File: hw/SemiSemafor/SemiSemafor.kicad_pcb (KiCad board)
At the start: 2 copper layers, 26.3 x 50.2 mm, 40 parts, among them J1 USB_PCB, J2 ESP-Programing_conector, SW1 SW_DIP_x01, SW2 SW_DIP_x01, U1 LD39200, U2 ESP32-C3-MINI-1

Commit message: 3D-models
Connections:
- D10 pad 1: Net-(D10-DOUT) -> Net-(D1-DOUT)
- D10 pad 3: Net-(D10-DIN) -> Net-(D1-DIN)
- D11 pad 1: Net-(D11-DOUT) -> Net-(D1-DOUT)
- D11 pad 3: Net-(D10-DOUT) -> Net-(D1-DIN)
- D12 pad 1: unconnected-(D12-DOUT-Pad1) -> Net-(D1-DOUT)
- D12 pad 3: Net-(D11-DOUT) -> Net-(D1-DIN)
- D2 pad 1: Net-(D2-DOUT) -> Net-(D1-DOUT)
- D2 pad 3: Net-(D1-DOUT) -> Net-(D1-DIN)
- D3 pad 1: Net-(D3-DOUT) -> Net-(D1-DOUT)
- D3 pad 3: Net-(D2-DOUT) -> Net-(D1-DIN)
- D4 pad 1: Net-(D4-DOUT) -> Net-(D1-DOUT)
- D4 pad 3: Net-(D3-DOUT) -> Net-(D1-DIN)
- D5 pad 1: Net-(D5-DOUT) -> Net-(D1-DOUT)
- D5 pad 3: Net-(D4-DOUT) -> Net-(D1-DIN)
- D6 pad 1: Net-(D6-DOUT) -> Net-(D1-DOUT)
- D6 pad 3: Net-(D5-DOUT) -> Net-(D1-DIN)
- D7 pad 1: Net-(D7-DOUT) -> Net-(D1-DOUT)
- D7 pad 3: Net-(D6-DOUT) -> Net-(D1-DIN)
- D8 pad 1: Net-(D8-DOUT) -> Net-(D1-DOUT)
- D8 pad 3: Net-(D7-DOUT) -> Net-(D1-DIN)
- D9 pad 1: Net-(D10-DIN) -> Net-(D1-DOUT)
- D9 pad 3: Net-(D8-DOUT) -> Net-(D1-DIN)

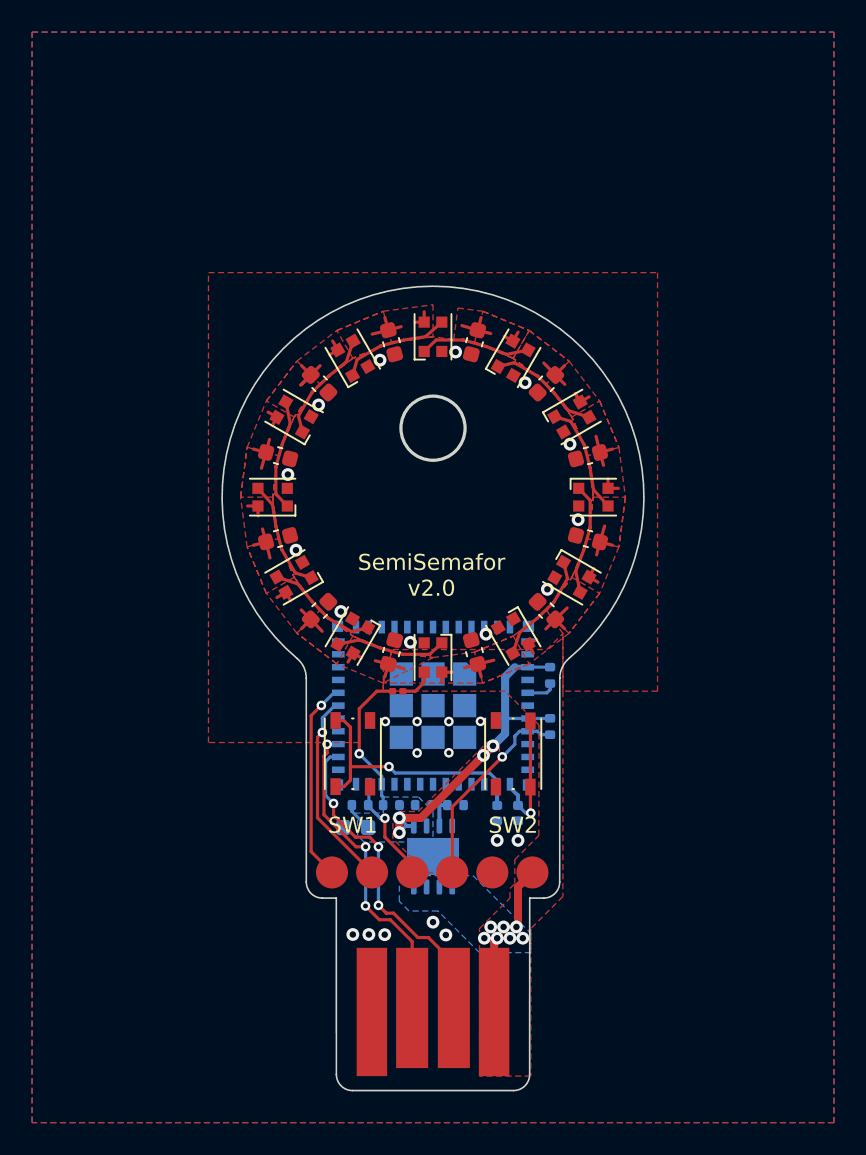
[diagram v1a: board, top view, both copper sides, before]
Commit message: Add IMU and move LED ring higher
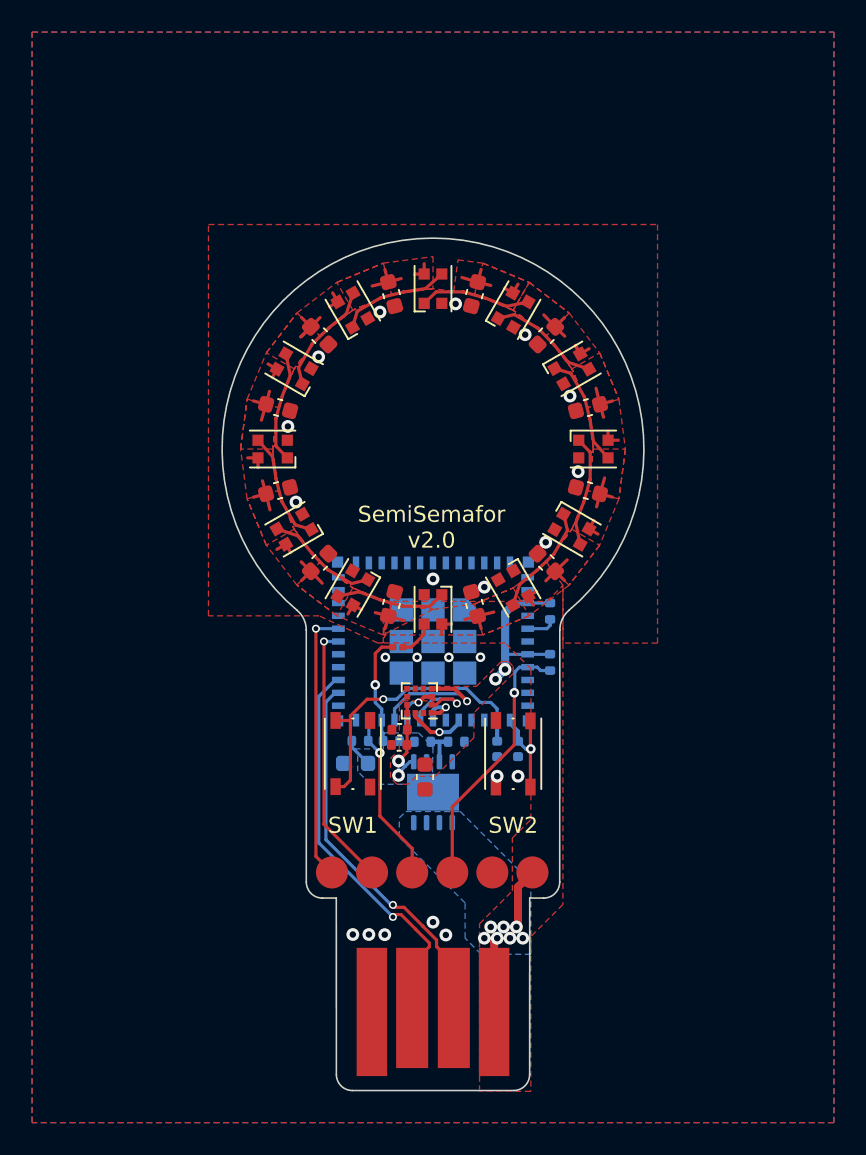
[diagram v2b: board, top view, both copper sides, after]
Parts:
- added C16: 10u, Capacitor_SMD:C_0603_1608Metric, F.Cu at (149.5, 103.5)
- added C17: 100n, Capacitor_SMD:C_0402_1005Metric, F.Cu at (147.9, 100.5)
- added C18: 100n, Capacitor_SMD:C_0402_1005Metric, F.Cu at (147.9, 101.5)
- added U3: LIS2DH12, Package_LGA:LGA-12_2x2mm_P0.5mm, F.Cu at (149.2, 98.7)
- C1, C10, C11, C12, C13, C14, C15, C2, C3, C4, C5, C9: value 1u -> 100n
- moved C6 4.00 mm to (145.2, 102.6)
- moved C7 4.00 mm to (154.0, 101.7)
- moved C8 4.00 mm to (155.3, 101.7)
- moved R2 4.00 mm to (145.4, 101.2)
- moved R3 4.00 mm to (147.4, 101.2)
- moved R4 4.00 mm to (157.3, 93.1)
- moved R5 4.00 mm to (157.3, 96.3)
- moved U1 4.00 mm to (150.0, 104.4)
- moved U2 4.00 mm to (150.0, 95.0)
- moved R10 3.95 mm to (151.4, 101.2)
- moved R11 3.95 mm to (149.3, 101.2)
- moved C1 3.00 mm to (147.4, 92.7)
- moved C10 3.00 mm to (152.6, 73.3)
- moved C11 3.00 mm to (147.4, 73.3)
- moved C12 3.00 mm to (142.9, 75.9)
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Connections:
- D10 pad 1: Net-(D1-DOUT) -> Net-(D10-DOUT)
- D10 pad 3: Net-(D1-DIN) -> Net-(D10-DIN)
- D11 pad 1: Net-(D1-DOUT) -> Net-(D11-DOUT)
- D11 pad 3: Net-(D1-DIN) -> Net-(D10-DOUT)
- D12 pad 1: Net-(D1-DOUT) -> unconnected-(D12-DOUT-Pad1)
- D12 pad 3: Net-(D1-DIN) -> Net-(D11-DOUT)
- D2 pad 1: Net-(D1-DOUT) -> Net-(D2-DOUT)
- D2 pad 3: Net-(D1-DIN) -> Net-(D1-DOUT)
- D3 pad 1: Net-(D1-DOUT) -> Net-(D3-DOUT)
- D3 pad 3: Net-(D1-DIN) -> Net-(D2-DOUT)
- D4 pad 1: Net-(D1-DOUT) -> Net-(D4-DOUT)
- D4 pad 3: Net-(D1-DIN) -> Net-(D3-DOUT)
- D5 pad 1: Net-(D1-DOUT) -> Net-(D5-DOUT)
- D5 pad 3: Net-(D1-DIN) -> Net-(D4-DOUT)
- D6 pad 1: Net-(D1-DOUT) -> Net-(D6-DOUT)
- D6 pad 3: Net-(D1-DIN) -> Net-(D5-DOUT)
- D7 pad 1: Net-(D1-DOUT) -> Net-(D7-DOUT)
- D7 pad 3: Net-(D1-DIN) -> Net-(D6-DOUT)
- D8 pad 1: Net-(D1-DOUT) -> Net-(D8-DOUT)
- D8 pad 3: Net-(D1-DIN) -> Net-(D7-DOUT)
- D9 pad 1: Net-(D1-DOUT) -> Net-(D10-DIN)
- D9 pad 3: Net-(D1-DIN) -> Net-(D8-DOUT)
- U2 pad 16: unconnected-(U2-GPIO10-Pad16) -> /IN1
- U2 pad 18: unconnected-(U2-GPIO4/ADC1_CH4-Pad18) -> /SPC
- U2 pad 19: unconnected-(U2-GPIO5/ADC1_CH0-Pad19) -> /CS
- U2 pad 20: unconnected-(U2-GPIO6-Pad20) -> /SDO
- U2 pad 21: unconnected-(U2-GPIO7-Pad21) -> /SDI
- U2 pad 7: +3.3V -> (no net)
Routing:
- net /SDI: track 0.00 -> 8.34 mm, vias 0 -> 1
- net +3.3V: track 24.9 -> 18.6 mm
- net /CS: track 0.00 -> 5.20 mm, vias 0 -> 1
- net /USB-D+: track 20.3 -> 24.9 mm, vias 3 -> 1
- net /TX0: track 12.6 -> 17.0 mm
- net /RX0: track 12.5 -> 16.5 mm
- net /EN: track 12.5 -> 16.5 mm
- net /BOOT: track 7.17 -> 11.0 mm
- net /IN1: track 0.00 -> 3.75 mm, vias 0 -> 1
- net /USB-D-: track 20.8 -> 23.8 mm, vias 3 -> 1
- net /SDO: track 0.00 -> 2.58 mm, vias 0 -> 1
- net /SPC: track 0.00 -> 2.51 mm, vias 0 -> 1
- net /I-LED: track 9.15 -> 6.90 mm
- net /SW1: track 16.6 -> 18.5 mm
- net /SW2: track 8.29 -> 6.65 mm
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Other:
- board size 26.3 x 50.2 mm -> 26.3 x 53.2 mm

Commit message: PCB extension
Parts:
- moved SW1 2.10 mm to (157.1, 102.0)
- moved SW2 2.10 mm to (142.9, 102.0), turned to 90 degrees
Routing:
- net /SW2: track 6.65 -> 14.4 mm
- net GND: track 0.00 -> 4.12 mm, vias 22 -> 26
- net /RX0: track 16.5 -> 19.3 mm
- net /TX0: track 17.0 -> 18.8 mm
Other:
- board size 26.3 x 53.2 mm -> 26.2 x 53.1 mm
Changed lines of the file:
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@@
   )
   (footprint "Button_Switch_SMD:SW_Push_1P1T_NO_Vertical_Wuerth_434133025816" (layer "F.Cu")
-    (at 155 102 90)
+    (at 157.1 102 90)
     (descr "https://katalog.we-online.com/em/datasheet/434133025816.pdf")
     (tags "tactile switch Wurth Wuerth")
@@
   )
   (footprint "Button_Switch_SMD:SW_Push_1P1T_NO_Vertical_Wuerth_434133025816" (layer "F.Cu")
-    (at 145 102 -90)
+    (at 142.9 102 90)
     (descr "https://katalog.we-online.com/em/datasheet/434133025816.pdf")
     (tags "tactile switch Wurth Wuerth")
@@
     (fp_arc (start 0.8 -1.099999) (mid 1.40384 0) (end 0.799999 1.099999)
       (stroke (width 0.1) (type solid)) (layer "F.Fab"))
-    (pad "1" smd rect (at -2.075 -1.075 270) (size 1.05 0.65) (layers "F.Cu" "F.Paste" "F.Mask")
+    (pad "1" smd rect (at -2.075 -1.075 90) (size 1.05 0.65) (layers "F.Cu" "F.Paste" "F.Mask")
       (net 2 "GND") (pintype "passive"))
-    (pad "1" smd rect (at 2.075 -1.075 270) (size 1.05 0.65) (layers "F.Cu" "F.Paste" "F.Mask")
+    (pad "1" smd rect (at 2.075 -1.075 90) (size 1.05 0.65) (layers "F.Cu" "F.Paste" "F.Mask")
       (net 2 "GND") (pintype "passive"))
-    (pad "2" smd rect (at -2.075 1.075 270) (size 1.05 0.65) (layers "F.Cu" "F.Paste" "F.Mask")
+    (pad "2" smd rect (at -2.075 1.075 90) (size 1.05 0.65) (layers "F.Cu" "F.Paste" "F.Mask")
       (net 9 "/SW1") (pintype "passive"))
-    (pad "2" smd rect (at 2.05 1.075 270) (size 1.05 0.65) (layers "F.Cu" "F.Paste" "F.Mask")
+    (pad "2" smd rect (at 2.05 1.075 90) (size 1.05 0.65) (layers "F.Cu" "F.Paste" "F.Mask")
       (net 9 "/SW1") (pintype "passive"))
     (model "${KICAD7_3DMODEL_DIR}/Button_Switch_SMD.3dshapes/SW_SPST_B3U-1000P.step"
@@
     )
   )
-  (gr_line (start 142.1 110) (end 142.096398 94.28)
+  (gr_line (start 136.9 111) (end 136.9 83)
     (stroke (width 0.1) (type solid)) (layer "Edge.Cuts"))
   (gr_arc (start 156.025 122) (mid 155.732107 122.707107) (end 155.025 123)
     (stroke (width 0.1) (type solid)) (layer "Edge.Cuts"))
-  (gr_line (start 157.908719 94.275683) (end 157.9 110)
+  (gr_line (start 163.1 83) (end 163.1 111)
     (stroke (width 0.1) (type solid)) (layer "Edge.Cuts"))
-  (gr_arc (start 157.908719 94.275683) (mid 158.059749 93.599708) (end 158.482337 93.050924)
-    (stroke (width 0.1) (type default)) (layer "Edge.Cuts"))
-  (gr_arc (start 141.52284 93.055291) (mid 149.996614 69.848152) (end 158.482337 93.050924)
-    (stroke (width 0.1) (type default)) (layer "Edge.Cuts"))
-  (gr_line (start 143.97 111) (end 143.1 111)
+  (gr_line (start 142.97 111) (end 136.9 111)
     (stroke (width 0.1) (type solid)) (layer "Edge.Cuts"))
   (gr_arc (start 144.975 123) (mid 144.267893 122.707107) (end 143.975 122)
     (stroke (width 0.1) (type solid)) (layer "Edge.Cuts"))
-  (gr_arc (start 157.9 110) (mid 157.607107 110.707107) (end 156.9 111)
+  (gr_arc (start 156.03 112) (mid 156.322893 111.292893) (end 157.03 111)
     (stroke (width 0.1) (type solid)) (layer "Edge.Cuts"))
+  (gr_arc (start 136.9 83) (mid 150 69.9) (end 163.1 83)
+    (stroke (width 0.1) (type default)) (layer "Edge.Cuts"))
   (gr_line (start 156.025 122) (end 156.03 111)
     (stroke (width 0.1) (type solid)) (layer "Edge.Cuts"))
-  (gr_arc (start 141.52284 93.055291) (mid 141.945389 93.604066) (end 142.096398 94.28)
-    (stroke (width 0.1) (type default)) (layer "Edge.Cuts"))
-  (gr_line (start 143.97 111) (end 143.975 122)
+  (gr_line (start 143.97 112) (end 143.975 122)
     (stroke (width 0.1) (type solid)) (layer "Edge.Cuts"))
-  (gr_arc (start 143.1 111) (mid 142.392893 110.707107) (end 142.1 110)
+  (gr_arc (start 142.97 111) (mid 143.677107 111.292893) (end 143.97 112)
     (stroke (width 0.1) (type solid)) (layer "Edge.Cuts"))
-  (gr_line (start 156.9 111) (end 156.03 111)
+  (gr_line (start 163.1 111) (end 157.03 111)
     (stroke (width 0.1) (type solid)) (layer "Edge.Cuts"))
   (gr_line (start 144.975 123) (end 155.025 123)
@@
   (via (at 153.2 113.5) (size 0.8) (drill 0.4) (layers "F.Cu" "B.Cu") (free) (net 1))
   (via (at 154 113.5) (size 0.8) (drill 0.4) (layers "F.Cu" "B.Cu") (free) (net 1))
+  (segment (start 156.075 99.95) (end 156.075 104.075) (width 0.2) (layer "F.Cu") (net 2))
   (via (at 159.05 84.41) (size 0.8) (drill 0.4) (layers "F.Cu" "B.Cu") (free) (net 2))
   (via (at 150 91.1) (size 0.8) (drill 0.4) (layers "F.Cu" "B.Cu") (free) (net 2))
+  (via (at 142.8 96.8) (size 0.8) (drill 0.4) (layers "F.Cu" "B.Cu") (free) (net 2))
   (via (at 155.3 103.4) (size 0.8) (drill 0.4) (layers "F.Cu" "B.Cu") (free) (net 2))
   (via (at 150 112.5) (size 0.8) (drill 0.4) (layers "F.Cu" "B.Cu") (free) (net 2))
+  (via (at 145.5 95.5) (size 0.8) (drill 0.4) (layers "F.Cu" "B.Cu") (free) (net 2))
   (via (at 155.746096 75.86747) (size 0.8) (drill 0.4) (layers "F.Cu" "B.Cu") (free) (net 2))
   (via (at 147.03 95.99) (size 0.6) (drill 0.3) (layers "F.Cu" "B.Cu") (free) (net 2))
@@
   (via (at 146.99 113.28) (size 0.8) (drill 0.4) (layers "F.Cu" "B.Cu") (free) (net 2))
   (via (at 146.696096 74.45747) (size 0.8) (drill 0.4) (layers "F.Cu" "B.Cu") (free) (net 2))
+  (via (at 145.5 97) (size 0.8) (drill 0.4) (layers "F.Cu" "B.Cu") (free) (net 2))
   (via (at 142.86747 77.253904) (size 0.8) (drill 0.4) (layers "F.Cu" "B.Cu") (free) (net 2))
   (via (at 150.8 113.3) (size 0.8) (drill 0.4) (layers "F.Cu" "B.Cu") (free) (net 2))
+  (via (at 141.8 97.8) (size 0.8) (drill 0.4) (layers "F.Cu" "B.Cu") (free) (net 2))
   (via (at 152.96 95.98) (size 0.6) (drill 0.3) (layers "F.Cu" "B.Cu") (free) (net 2))
   (segment (start 147.85 102.45) (end 148.37 101.93) (width 0.2) (layer "F.Cu") (net 3))
@@
   (segment (start 142.875 107.55) (end 147.5 112.175) (width 0.2) (layer "B.Cu") (net 6))
   (segment (start 142.875 98.425) (end 142.875 107.55) (width 0.2) (layer "B.Cu") (net 6))
-  (segment (start 156.075 99.95) (end 156.075 104.075) (width 0.2) (layer "F.Cu") (net 7))
-  (via (at 156.1 101.7) (size 0.6) (drill 0.3) (layers "F.Cu" "B.Cu") (net 7))
+  (segment (start 158.175 104.075) (end 158.175 101.8) (width 0.2) (layer "F.Cu") (net 7))
+  (segment (start 158.8 101.8) (end 158.175 101.8) (width 0.25) (layer "F.Cu") (net 7))
+  (segment (start 158.175 99.95) (end 158.175 104.075) (width 0.25) (layer "F.Cu") (net 7))
+  (segment (start 158.175 101.8) (end 158.175 99.95) (width 0.2) (layer "F.Cu") (net 7))
+  (via (at 158.8 101.8) (size 0.8) (drill 0.4) (layers "F.Cu" "B.Cu") (net 7))
   (segment (start 154.8 100.1) (end 154.8 99.9) (width 0.25) (layer "B.Cu") (net 7))
   (segment (start 155.3 100.6) (end 154.8 100.1) (width 0.25) (layer "B.Cu") (net 7))
-  (segment (start 156.1 101.7) (end 155.78 101.7) (width 0.2) (layer "B.Cu") (net 7))
-  (segment (start 155.78 101.7) (end 155.3 101.22) (width 0.2) (layer "B.Cu") (net 7))
+  (segment (start 157.6 100.6) (end 158.8 101.8) (width 0.25) (layer "B.Cu") (net 7))
   (segment (start 155.3 101.22) (end 155.3 100.6) (width 0.25) (layer "B.Cu") (net 7))
+  (segment (start 155.3 100.6) (end 157.6 100.6) (width 0.25) (layer "B.Cu") (net 7))
   (segment (start 155.9 94.2) (end 157.1 94.2) (width 0.2) (layer "B.Cu") (net 8))
   (segment (start 157.1 94.2) (end 157.3 94) (width 0.2) (layer "B.Cu") (net 8))
@@
   (segment (start 146.685086 101.943355) (end 145.96 101.218269) (width 0.2) (layer "B.Cu") (net 12))
   (segment (start 145.96 101.218269) (end 145.96 101.2) (width 0.2) (layer "B.Cu") (net 12))
-  (segment (start 143.7 109.4) (end 142.7 108.4) (width 0.2) (layer "F.Cu") (net 13))
-  (segment (start 142.7 108.4) (end 142.7 94.2) (width 0.2) (layer "F.Cu") (net 13))
+  (segment (start 140.5 106.2) (end 140.5 96.4) (width 0.2) (layer "F.Cu") (net 13))
+  (segment (start 140.5 96.4) (end 142.7 94.2) (width 0.2) (layer "F.Cu") (net 13))
+  (segment (start 143.7 109.4) (end 140.5 106.2) (width 0.2) (layer "F.Cu") (net 13))
   (via (at 142.7 94.2) (size 0.5) (drill 0.3) (layers "F.Cu" "B.Cu") (net 13))
   (segment (start 142.7 94.2) (end 144.1 94.2) (width 0.2) (layer "B.Cu") (net 13))
-  (segment (start 146.2 109.4) (end 143.2 106.4) (width 0.2) (layer "F.Cu") (net 14))
-  (segment (start 143.2 106.4) (end 143.2 95) (width 0.2) (layer "F.Cu") (net 14))
+  (segment (start 140.83 105.33) (end 140.83 97.37) (width 0.2) (layer "F.Cu") (net 14))
+  (segment (start 142.5 107) (end 140.83 105.33) (width 0.2) (layer "F.Cu") (net 14))
+  (segment (start 146.2 109.4) (end 143.8 107) (width 0.2) (layer "F.Cu") (net 14))
+  (segment (start 140.83 97.37) (end 143.2 95) (width 0.2) (layer "F.Cu") (net 14))
+  (segment (start 143.8 107) (end 142.5 107) (width 0.2) (layer "F.Cu") (net 14))
   (via (at 143.2 95) (size 0.5) (drill 0.3) (layers "F.Cu" "B.Cu") (net 14))
   (segment (start 143.2 95) (end 144.1 95) (width 0.2) (layer "B.Cu") (net 14))
@@
     (polygon
       (pts
-        (xy 158.1 95.097485)
+        (xy 158.1 111.397485)
         (xy 158.1 91.5)
         (xy 157.07 90.07)
@@
         (xy 136 69)
         (xy 164 69)
-        (xy 164 95.1)
+        (xy 164 111.4)
       )
     )

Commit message: Correction
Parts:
- added G***: LOGO, LOGO, F.Cu at (150.0, 83.0)
- moved SW1 2.10 mm to (155.0, 102.0)
- moved SW2 2.10 mm to (145.0, 102.0), turned to -90 degrees
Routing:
- net /SW2: track 14.4 -> 7.41 mm
- net GND: track 4.12 -> 0.00 mm, vias 26 -> 28
- net /RX0: track 19.3 -> 17.3 mm
- net /TX0: track 18.8 -> 17.5 mm
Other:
- outline, holes or cut-outs redrawn
- board text added: "SemiSemafor v2.1.0 vzorek.com/semisemafor"
- board text removed: "SemiSemafor v2.0"

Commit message: v2.1.0
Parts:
- added J3: Conn_01x02, RKL-ESP:ESP-Small-programming connector, B.Cu at (150.0, 119.0)
- added REF**: Tab, kikit:Tab, F.Cu at (150.0, 123.2)
- added REF**: Tab, kikit:Tab, F.Cu at (163.3, 93.9)
- added REF**: Tab, kikit:Tab, F.Cu at (136.7, 93.9)
- added REF**: Tab, kikit:Tab, F.Cu at (150.1, 69.7)
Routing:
- net GND: track 0.00 -> 15.7 mm
- net /EN: track 16.5 -> 26.3 mm, vias 1 -> 2
- net /BOOT: track 11.0 -> 20.7 mm, vias 1 -> 2
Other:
- board text added: "EN BOOT"
- board text added: "T R B EN G 5"
